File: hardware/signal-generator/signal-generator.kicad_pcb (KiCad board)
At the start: 4 copper layers, 152 parts, among them J1 AVR-ISP-6, J10 Output_Conn, J11 SD_Card_Conn, J12 TP_Conn, J13 LCD_Conn, J2 AVR_SPI, J3 PORT_G, J4 PORT_F, J5 PORT_E, J6 PORT_A, J7 PORT_C, J8 AREF, J9 Power_Supply_Rails, Q1 MMBF5485, Q10 AP2310GN, Q11 AP2310GN, Q12 AP2310GN, Q2 MMBF5485, Q3 MMBF5485, Q4 AP2310GN, Q5 AP2310GN, Q6 AP2310GN, Q7 AP2310GN, Q8 AP2310GN, Q9 AP2310GN, SW1 RESET_BUTTON, U1 74HC04, U10 MCP23017-E/SO, U11 AD9764AR, U12 TS4061AICT-1.25, U13 74HC4040, U14 74HC4040, U15 MCP4551-103E/MS, U16 AD8021ARZ, U17 AD8021ARZ, U18 MCP4716, U19 AD8021ARZ, U2 74HC08, U20 MIC6211, U21 AZ431AN-A, U22 AD8021ARZ, U3 74HC08, U4 74HC30, U5 ATmega2561-16AU, U6 ADP7142AUJZ-5.0, U7 TC1017-3.3VCTTR, U8 DS1085Z-10+, U9 CY7C1021D-10ZSXI, Y1 16MHz

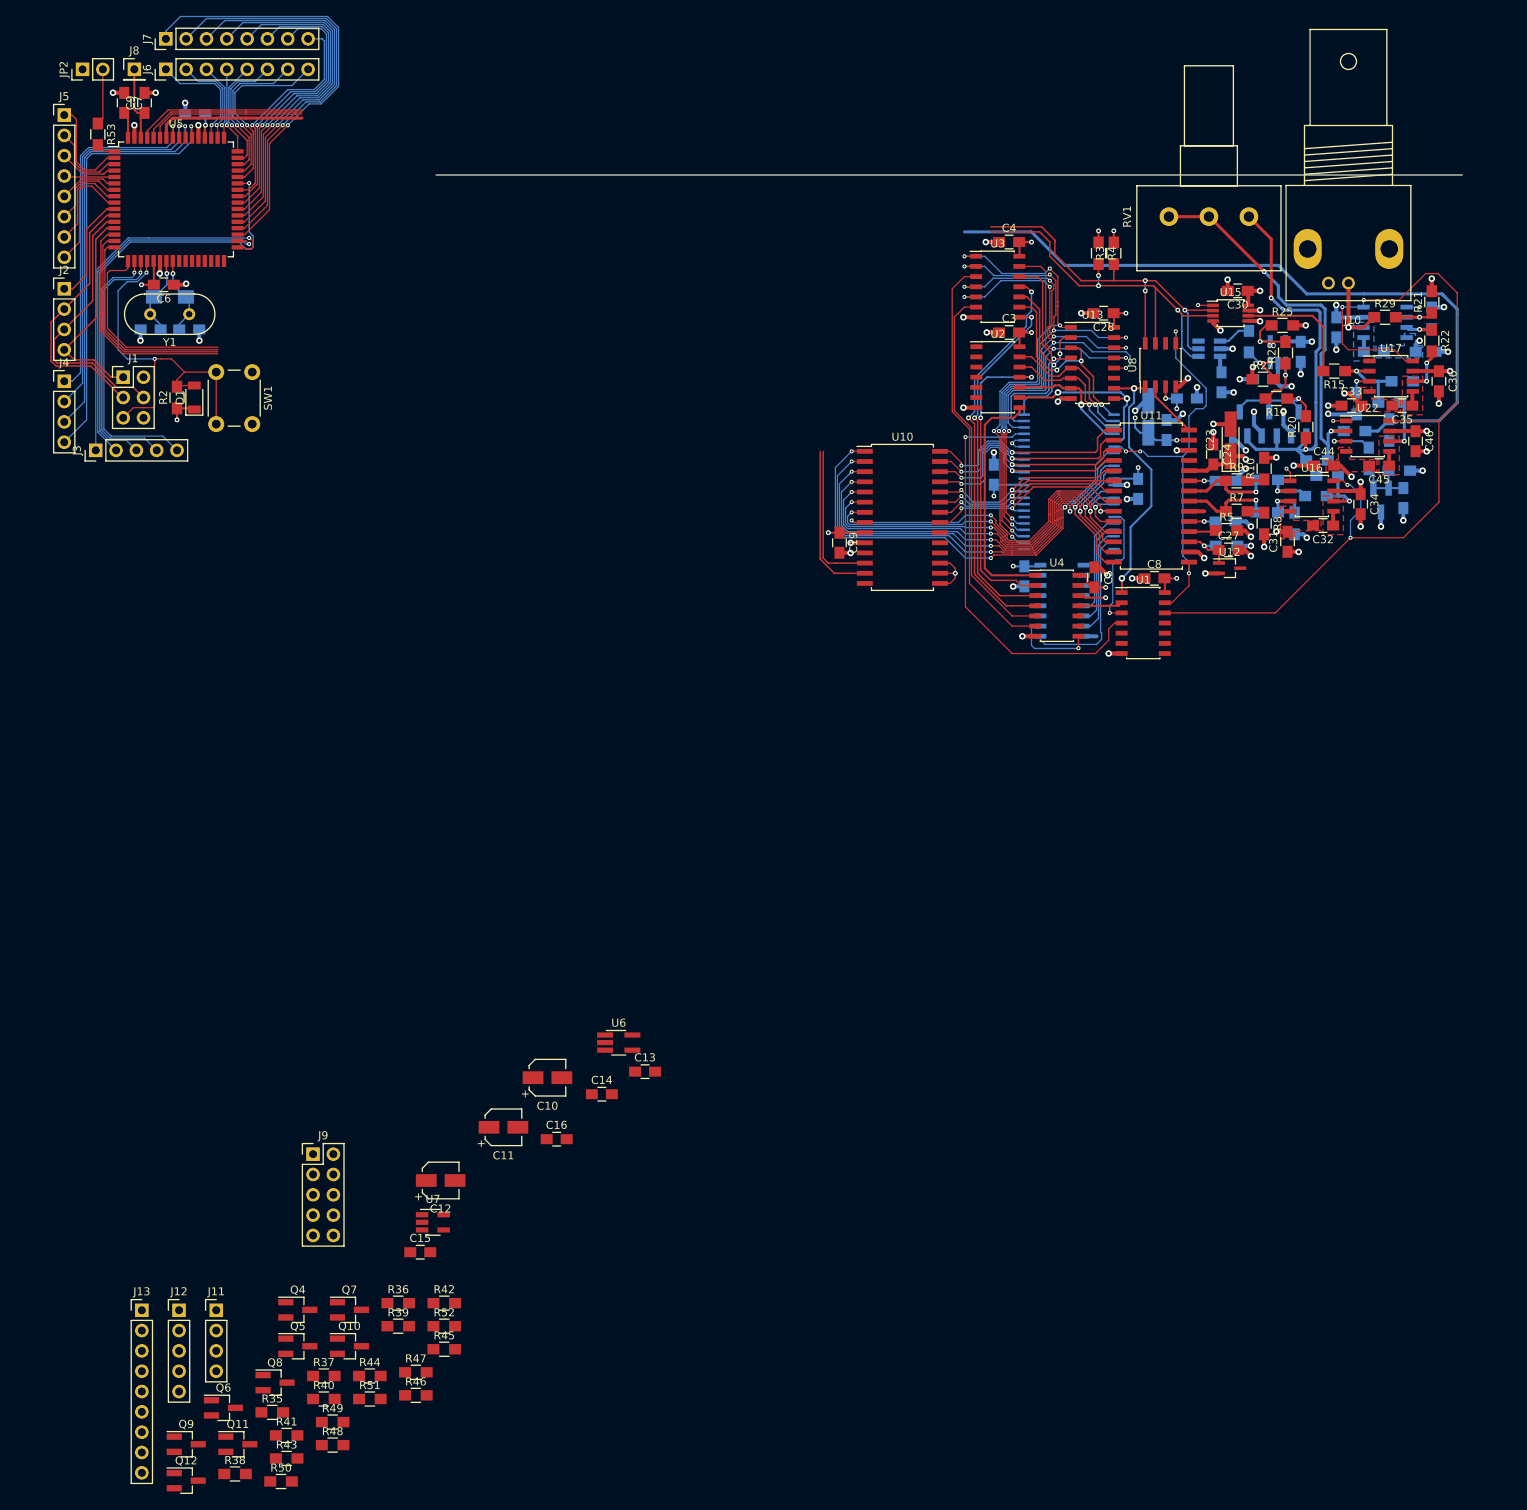
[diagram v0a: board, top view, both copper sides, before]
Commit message: [Signal Generator] Route TFT LCD interface circuitry
This circuitry includes the level shifters as well as the pin headers to
the LCD.
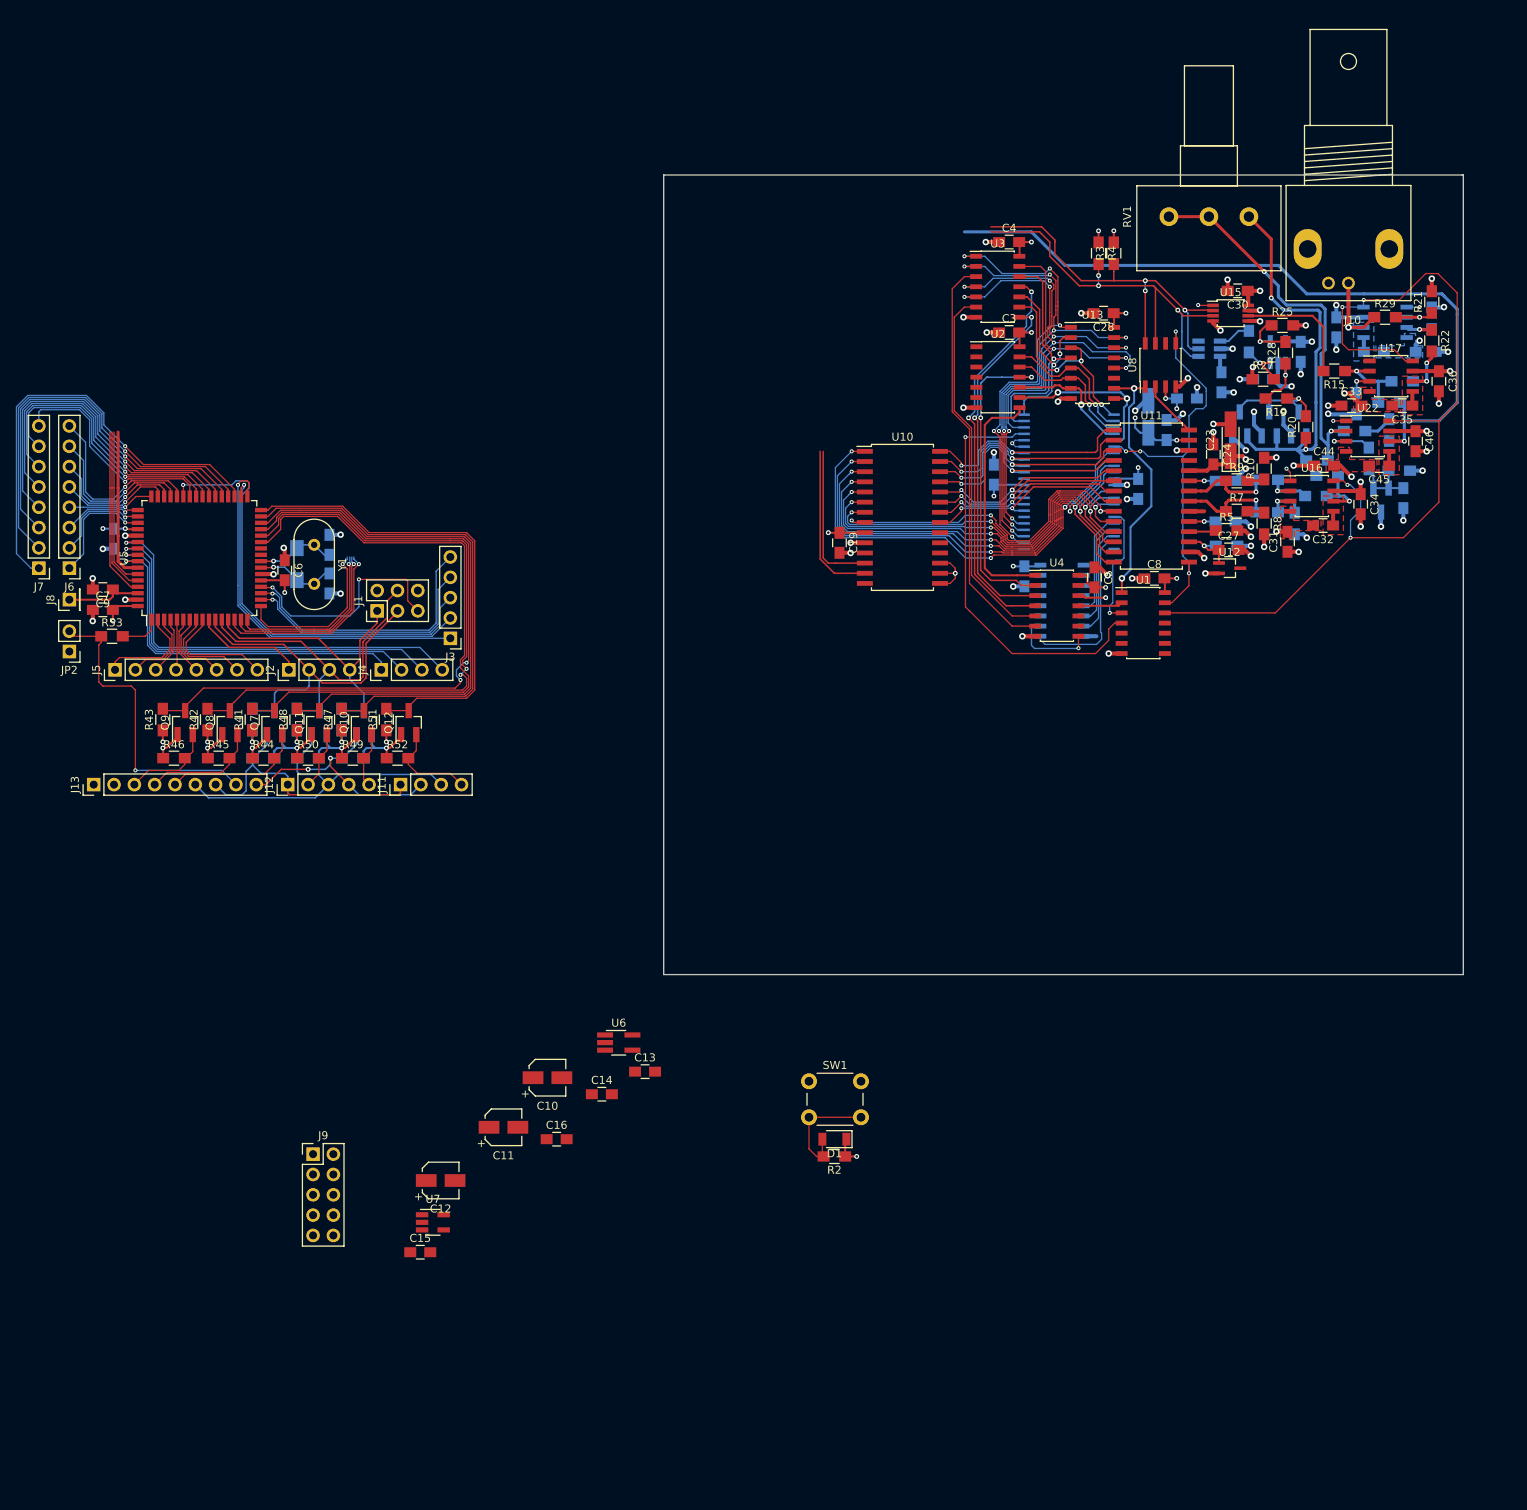
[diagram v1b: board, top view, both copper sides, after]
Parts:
- Q4, Q5, Q6, R35, R36, R37, R38, R39, R40: moved to B.Cu
- moved R2 125.5 mm to (117.9, 155.2), turned to 180 degrees
- moved D1 122.5 mm to (117.9, 153.0), turned to 180 degrees
- moved SW1 112.7 mm to (114.7, 145.8), turned to 0 degrees
- moved Q12 98.7 mm to (64.6, 101.0), turned to 90 degrees
- moved R43 93.6 mm to (33.9, 100.6), turned to 90 degrees
- moved R48 90.8 mm to (50.7, 100.6), turned to 90 degrees
- moved Q11 90.8 mm to (53.5, 101.0), turned to 90 degrees
- moved R38 90.7 mm to (57.7, 105.4), turned to 180 degrees
- moved R50 90.5 mm to (52.1, 105.4)
- moved Q9 90.2 mm to (36.7, 101.0), turned to 90 degrees
- moved R41 89.6 mm to (45.1, 100.6), turned to 90 degrees
- moved R35 87.0 mm to (56.3, 100.6), turned to 90 degrees
- moved Q6 86.5 mm to (53.5, 101.0), turned to 90 degrees
- moved R46 85.2 mm to (35.3, 105.4)
- moved R51 85.0 mm to (61.8, 100.6), turned to 90 degrees
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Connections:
- J11 pad 1: /TFT LCD Module Interface Block/SD_~CS -> /TFT LCD Module Interface Block/SCK_3.3
- J11 pad 2: /TFT LCD Module Interface Block/MOSI_3.3 -> /TFT LCD Module Interface Block/MISO_3.3
- J11 pad 3: /TFT LCD Module Interface Block/MISO_3.3 -> /TFT LCD Module Interface Block/MOSI_3.3
- J11 pad 4: /TFT LCD Module Interface Block/SCK_3.3 -> /TFT LCD Module Interface Block/SD_~CS
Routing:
- net /~CS~_LCD: track 0.00 -> 86.2 mm, vias 0 -> 2
- net /~RESET~_LCD: track 0.00 -> 81.8 mm, vias 0 -> 2
- net /DC\~RS~_LCD: track 0.00 -> 76.0 mm
- net /~CS~_T: track 0.00 -> 70.0 mm
- net /IRQ_T: track 0.00 -> 64.9 mm
- net /~CS~_SD: track 0.00 -> 59.9 mm
- net /TFT LCD Module Interface Block/MOSI_3.3: track 0.00 -> 43.2 mm
- net +3V3: track 0.00 -> 41.2 mm, vias 0 -> 6
- net /TFT LCD Module Interface Block/SCK_3.3: track 0.00 -> 35.1 mm
- net /TFT LCD Module Interface Block/LCD_BL: track 7.04 -> 38.4 mm, vias 0 -> 1
- net /TFT LCD Module Interface Block/MISO_3.3: track 0.00 -> 30.6 mm, vias 0 -> 2
- net /TFT LCD Module Interface Block/LCD_DC\~RS: track 0.00 -> 17.6 mm
- net +5VD: track 69.4 -> 85.2 mm, vias 19 -> 27
- net /TFT LCD Module Interface Block/LCD_~RESET: track 0.00 -> 14.6 mm
- net /TFT LCD Module Interface Block/SD_~CS: track 0.00 -> 11.9 mm
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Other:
- board outline added: 99.9 x 99.9 mm

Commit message: [Signal Generator] Connect all digital signal lines
The microcontroller is now properly positioned on the PCB and all of the
digital signal tracks have been completed.
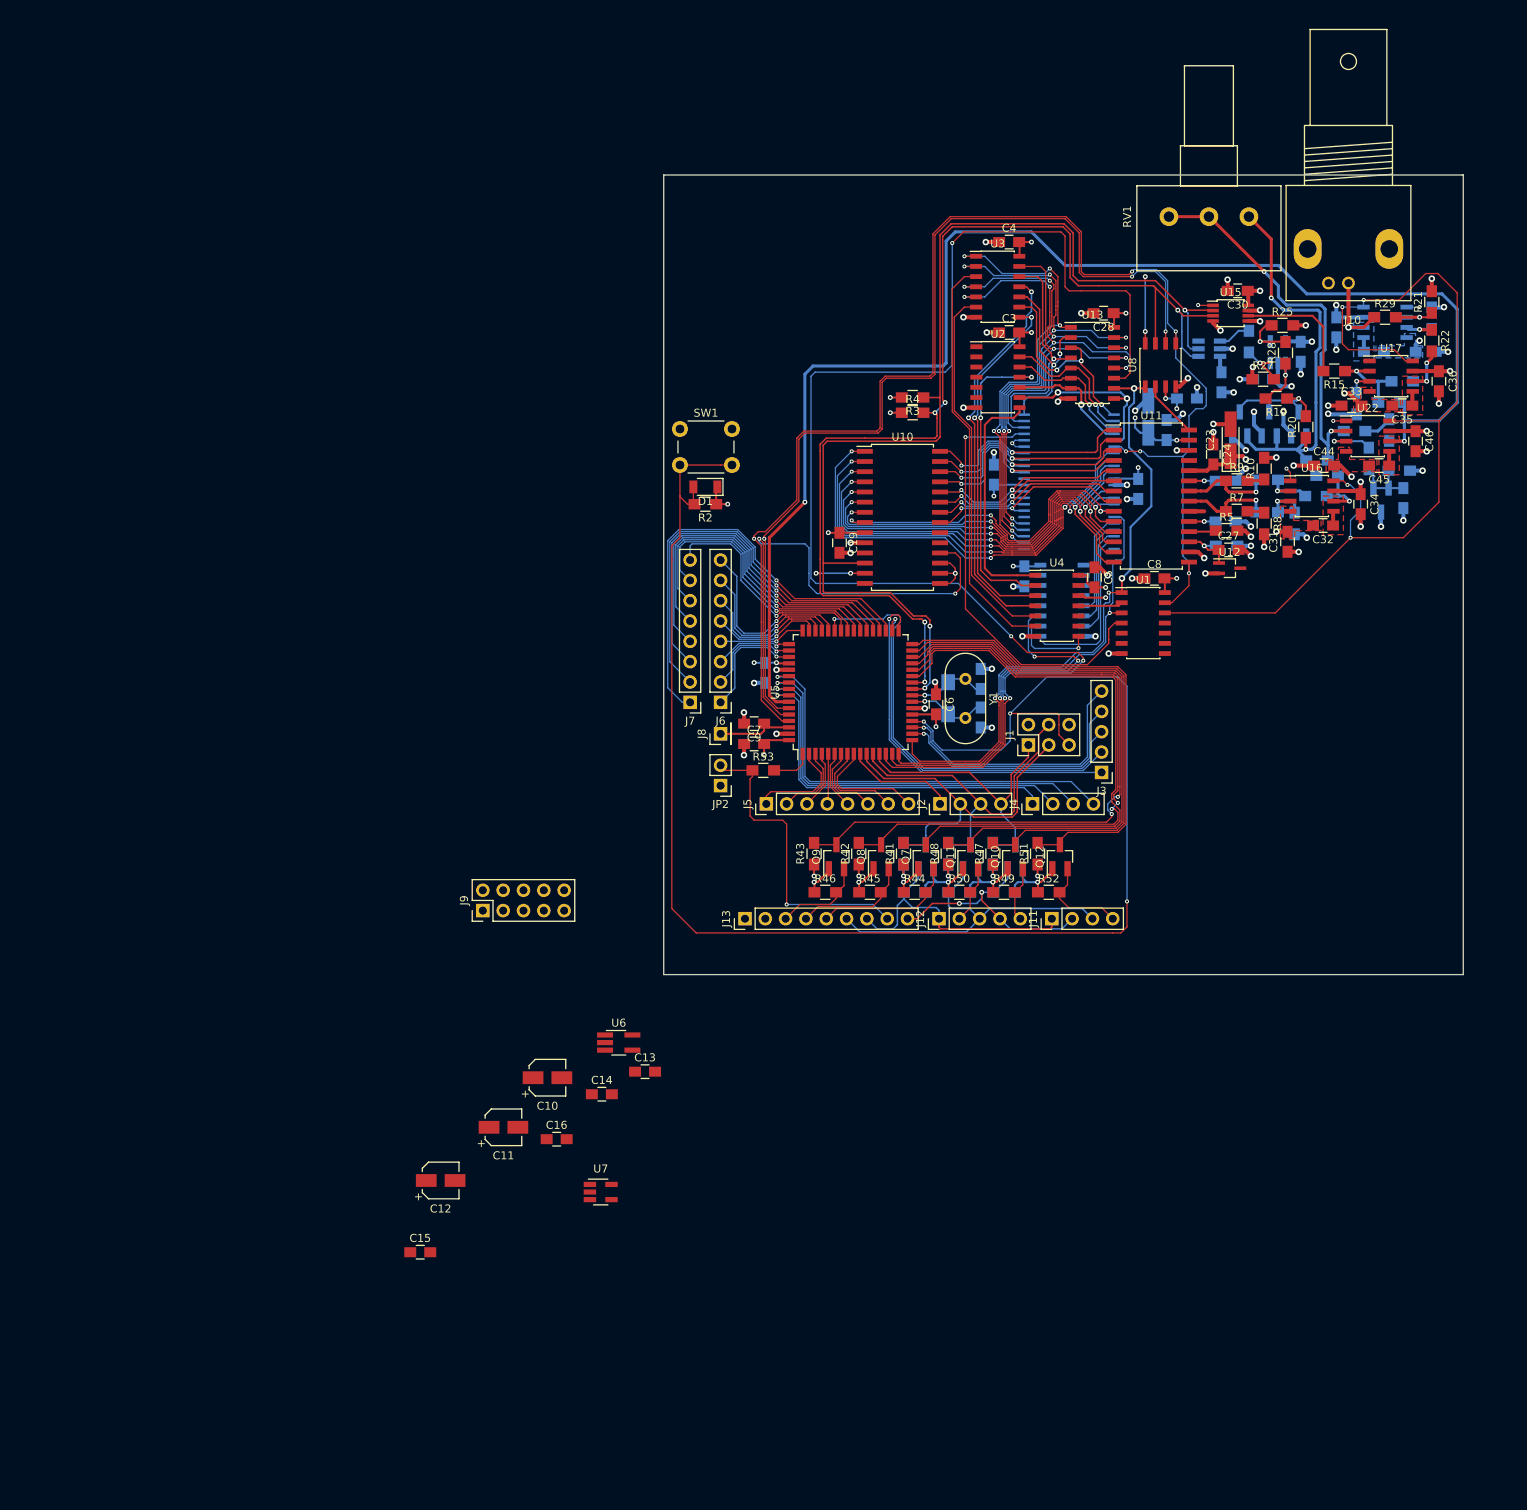
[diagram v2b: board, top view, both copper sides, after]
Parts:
- moved C1 83.1 mm to (136.1, 95.5)
- moved C2 83.1 mm to (136.1, 100.3)
- moved C6 83.1 mm to (130.6, 98.7)
- moved J12 83.1 mm to (130.9, 125.5)
- moved J13 83.1 mm to (106.7, 125.5)
- moved J3 83.1 mm to (151.3, 107.2)
- moved J4 83.1 mm to (142.6, 111.1)
- moved J6 83.1 mm to (103.6, 98.4)
- moved J7 83.1 mm to (99.8, 98.4)
- moved J8 83.1 mm to (103.6, 102.4)
- moved JP2 83.1 mm to (103.6, 108.8)
- moved Q12 83.1 mm to (146.1, 117.7)
- moved Q5 83.1 mm to (129.3, 117.7)
- moved Q7 83.1 mm to (129.3, 117.7)
- moved R1 83.1 mm to (132.1, 97.9)
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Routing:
- net /~RESET: track 43.7 -> 201.2 mm, vias 2 -> 3
- net /~CMR1: track 24.5 -> 175.9 mm, vias 1 -> 4
- net /PWRDWN: track 72.6 -> 176.6 mm, vias 4 -> 6
- net /~OSCOE: track 19.8 -> 122.8 mm, vias 0 -> 3
- net /SCL: track 68.0 -> 148.3 mm, vias 3 -> 5
- net /SDA: track 70.4 -> 147.9 mm, vias 3 -> 7
- net /OCAL: track 112.6 -> 174.7 mm, vias 1 -> 2
- net /~IOExRESET: track 20.5 -> 62.0 mm, vias 0 -> 2
- net /~CP: track 53.2 -> 78.4 mm, vias 3 -> 4
- net /~CMR2: track 22.9 -> 47.1 mm, vias 1 -> 3
- net /R\~W: track 37.1 -> 57.7 mm
- net Net-(U1-Pad4): track 53.1 -> 54.7 mm
- net AGND: track 128.9 -> 128.8 mm, vias 68 -> 69

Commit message: [Signal Generator] Complete board layout
All components are appropriately positioned and connected.

The only thing left to do is to layout the supply rails, as well as the
two ground planes.
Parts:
- added REF**: MountingHole_3mm, Mounting_Holes:MountingHole_3mm, F.Cu at (106.3, 149.9)
- added REF**: MountingHole_3mm, Mounting_Holes:MountingHole_3mm, F.Cu at (198.6, 149.9)
- added REF**: MountingHole_3mm, Mounting_Holes:MountingHole_3mm, F.Cu at (106.3, 57.5)
- added REF**: MountingHole_3mm, Mounting_Holes:MountingHole_3mm, F.Cu at (198.6, 57.5)
- C13, C14, C15, C16, U6, U7: moved to B.Cu
- moved C16 115.0 mm to (196.1, 131.4), turned to 90 degrees
- moved C12 107.8 mm to (170.9, 124.3), turned to 90 degrees
- moved C15 104.8 mm to (163.4, 128.3)
- moved C11 104.3 mm to (179.8, 137.5), turned to 90 degrees
- moved U6 101.7 mm to (192.2, 130.9)
- moved C10 100.1 mm to (179.8, 124.3), turned to 90 degrees
- moved J9 96.1 mm to (169.7, 132.2)
- moved C13 94.9 mm to (188.2, 131.4), turned to 90 degrees
- moved U7 80.1 mm to (163.4, 131.1), turned to 180 degrees
- moved C14 75.9 mm to (163.4, 133.9), turned to 180 degrees
- moved C20 22.0 mm to (143.8, 91.2)
- moved C21 22.0 mm to (163.1, 83.9)
- moved C22 22.0 mm to (165.4, 85.6)
- moved C3 22.0 mm to (145.7, 73.4)
- moved C31 22.0 mm to (180.5, 99.6)
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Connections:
- J9 pad 1: +12VA -> AGND
- J9 pad 10: AGND -> +12VA
- J9 pad 2: -12VA -> +5VD
- J9 pad 4: AGND -> +5VD
- J9 pad 7: +5VD -> AGND
- J9 pad 9: +5VD -> -12VA
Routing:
- net AGND: track 128.8 -> 144.9 mm, vias 69 -> 77
- net +5VD: track 85.2 -> 98.4 mm, vias 27 -> 29
- net +12VA: track 22.8 -> 31.1 mm, vias 5 -> 7
- net -12VA: track 13.5 -> 20.3 mm, vias 5 -> 6
- net +3V3: track 41.2 -> 44.5 mm, vias 6 -> 7
- net /~RESET: track 201.2 -> 198.7 mm
- net +5VA: track 25.5 -> 27.1 mm, vias 9 -> 10
- net Net-(R31-Pad1): track 50.0 -> 51.1 mm
- added copper zone on B.Cu, net +12VA
- added copper zone on B.Cu, net +5VA
- added copper zone on F.Cu, net +5VD
- added copper zone on B.Cu, net AGND

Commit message: [Signal Generator] Provide power to all components
The board's power supply rails are laid.
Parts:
- moved C42 0.76 mm to (186.6, 73.5)
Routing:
- net +5VD: track 98.4 -> 481.8 mm
- net +5VA: track 27.1 -> 187.8 mm, vias 10 -> 11
- net +3V3: track 44.5 -> 179.8 mm
- net +12VA: track 31.1 -> 131.1 mm
- net -12VA: track 20.3 -> 104.4 mm

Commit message: [Signal Generator] Layout AGND and DGND ground planes
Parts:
- moved C8 0.51 mm to (163.3, 104.1)
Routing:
- net AGND: track 145.1 -> 149.6 mm, vias 77 -> 79
- net +5VD: track 481.8 -> 478.5 mm
- added copper zone on In2.Cu, net AGND

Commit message: [Signal Generator] Finish PCB
This commit includes the following changes:
- Reorder component references on F.Silk and B.Silk layers;
- Include additional texts on F.Silk and B.Silk layers;
- Add 'ELSYS' logo on F.Silk layer;
- Add keepout zones around 3mm mounting holes;
- Add board dimensions on F.Fab layer.
With these final changes this PCB is ready to be manufactured.
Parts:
- added G***: LOGO, elsys-logo:elsys-logo, F.Cu at (119.0, 71.5)
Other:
- board text added: "+12VA"
- board text added: "+5VD"
- board text added: "-12VA"
- board text added: "2020"
- board text added: "AGND"
- board text added: "AREF"
- board text added: "AVR ISP"
- board text added: "AVR SPI"
- board text added: "DESIGN BY PETAR NIKOLOV"
- board text added: "DGND"
- board text added: "DIGITAL FUNCTION GENERATOR V2"
- board text added: "LCD"
- board text added: "NC"
- board text added: "ON BL"
- board text added: "PORT A"
- board text added: "PORT C"
- board text added: "PORT E"
- board text added: "PORT F"
- board text added: "PORT G"
- board text added: "RESET"
- board text added: "SD CARD"
- board text added: "TOUCH PANEL"
- board text added: "VOUT"
